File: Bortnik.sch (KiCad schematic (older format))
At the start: 1 part

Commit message: Up
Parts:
- added X?: СНП58-64-МПИ, symbol 180x:СНП58-64-МПИ
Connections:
- new net: X?.A2 (GND), X?.A3 (GND)
- new net: X?.B2 (GND), X?.B3 (GND)
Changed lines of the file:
@@
 	1    0    0    -1
 $EndComp
+$Comp
+L 180x:СНП58-64-МПИ X?
+U 1 1 61B01EB3
+P 2450 3675
+F 0 "X?" H 2450 5400 50  0000 C CNN
+F 1 "СНП58-64-МПИ" H 2450 5309 50  0000 C CNN
+F 2 "" H 2000 3675 50  0001 C CNN
+F 3 "" H 2000 3675 50  0001 C CNN
+	1    2450 3675
+	1    0    0    -1
+$EndComp
+Text GLabel 1225 4050 0    50   BiDi ~ 0
+IRQ3
+Text GLabel 1225 4175 0    50   BiDi ~ 0
+IRQ2
+Text GLabel 1225 4300 0    50   BiDi ~ 0
+IRQ1
+Text GLabel 1225 4425 0    50   BiDi ~ 0
+IRQ0
+Wire Wire Line
+	2950 2275 3100 2275
+Wire Wire Line
+	3100 2275 3100 2375
+Wire Wire Line
+	3100 2375 2950 2375
+Wire Wire Line
+	1950 2275 1825 2275
+Wire Wire Line
+	1825 2275 1825 2375
+Wire Wire Line
+	1825 2375 1950 2375
 $EndSCHEMATC

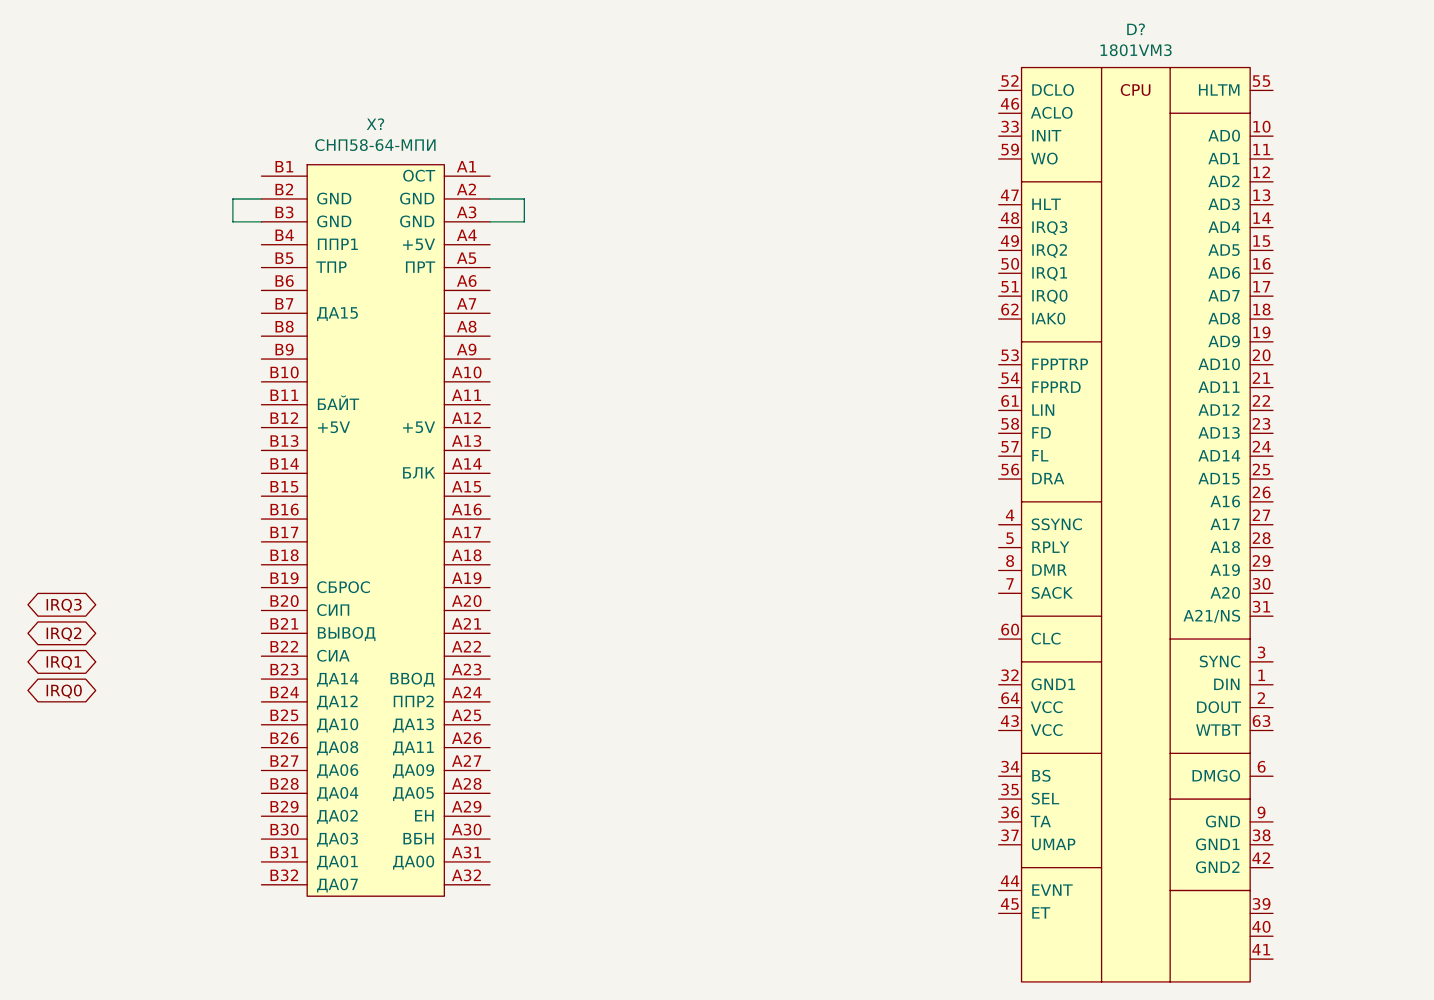
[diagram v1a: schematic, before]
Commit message: Update for Peripheral connector
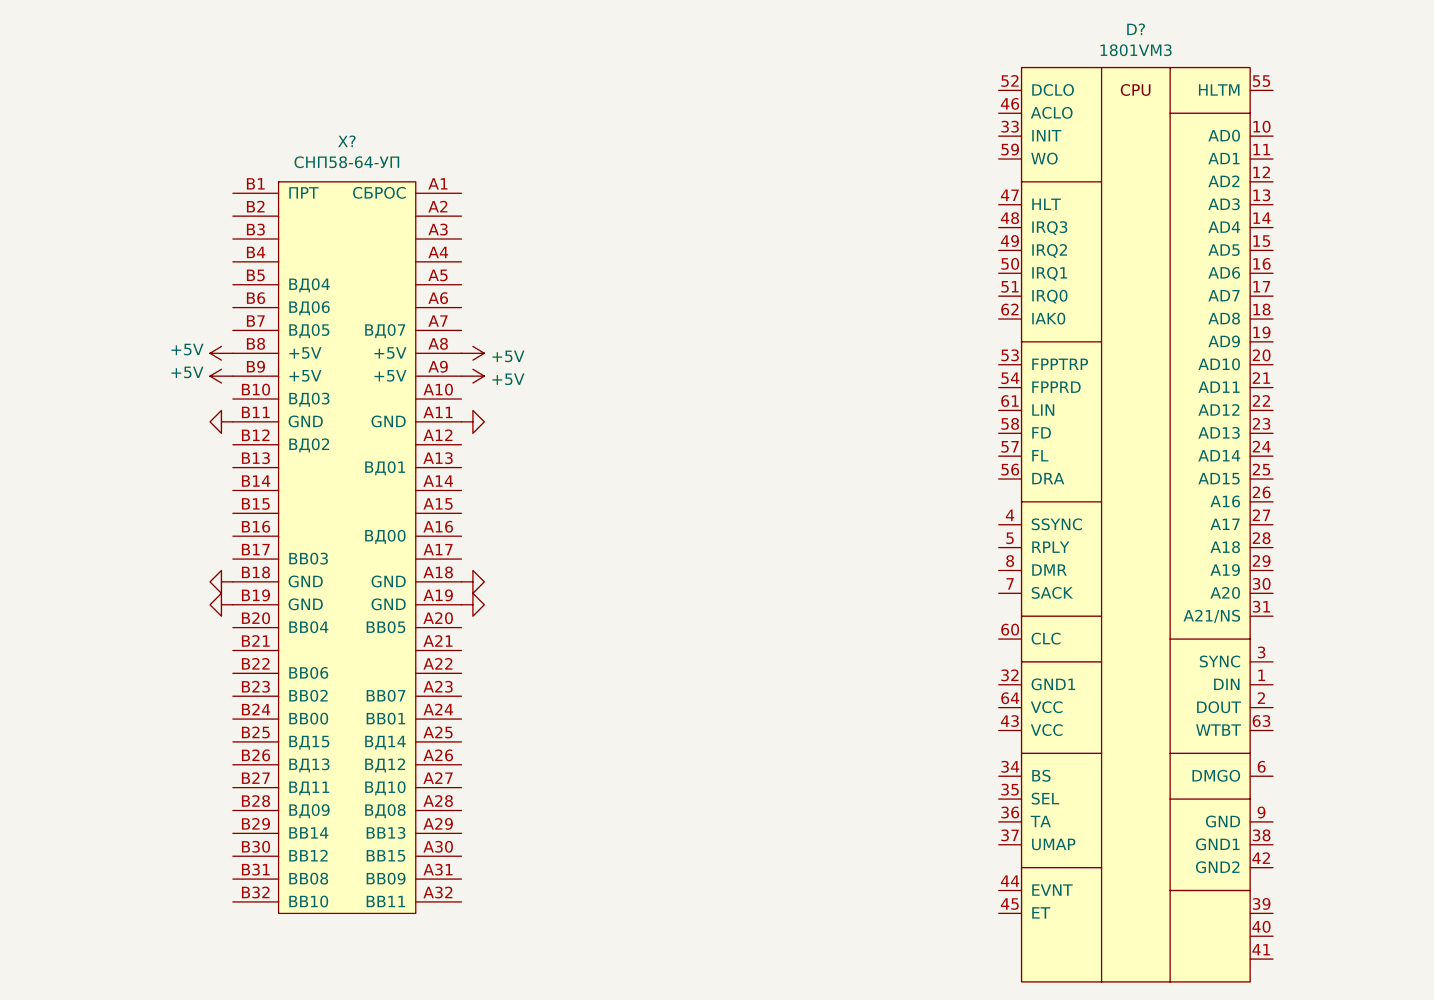
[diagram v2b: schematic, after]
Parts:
- removed X?: СНП58-64-МПИ, symbol 180x:СНП58-64-МПИ
- added X?: СНП58-64-УП, symbol 180x:СНП58-64-УП
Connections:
- new net +5V: X?.A8 (+5V), X?.A9 (+5V), X?.B8 (+5V), X?.B9 (+5V)
- new net GND: X?.A11 (GND), X?.A18 (GND), X?.A19 (GND), X?.B11 (GND), X?.B18 (GND), X?.B19 (GND)
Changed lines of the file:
@@
 $EndComp
 $Comp
-L 180x:СНП58-64-МПИ X?
-U 1 1 61B01EB3
-P 2450 3675
-F 0 "X?" H 2450 5400 50  0000 C CNN
-F 1 "СНП58-64-МПИ" H 2450 5309 50  0000 C CNN
-F 2 "" H 2000 3675 50  0001 C CNN
-F 3 "" H 2000 3675 50  0001 C CNN
-	1    2450 3675
+L power:+5V #PWR?
+U 1 1 61B662BF
+P 1825 3050
+F 0 "#PWR?" H 1825 2900 50  0001 C CNN
+F 1 "+5V" V 1840 3178 50  0000 L CNN
+F 2 "" H 1825 3050 50  0001 C CNN
+F 3 "" H 1825 3050 50  0001 C CNN
+	1    1825 3050
+	0    -1   -1   0
+$EndComp
+$Comp
+L power:+5V #PWR?
+U 1 1 61B65EB9
+P 1825 2950
+F 0 "#PWR?" H 1825 2800 50  0001 C CNN
+F 1 "+5V" V 1840 3078 50  0000 L CNN
+F 2 "" H 1825 2950 50  0001 C CNN
+F 3 "" H 1825 2950 50  0001 C CNN
+	1    1825 2950
+	0    -1   -1   0
+$EndComp
+$Comp
+L power:+5V #PWR?
+U 1 1 61B6590B
+P 2825 3050
+F 0 "#PWR?" H 2825 2900 50  0001 C CNN
+F 1 "+5V" V 2840 3178 50  0000 L CNN
+F 2 "" H 2825 3050 50  0001 C CNN
+F 3 "" H 2825 3050 50  0001 C CNN
+	1    2825 3050
+	0    1    1    0
+$EndComp
+$Comp
+L power:+5V #PWR?
+U 1 1 61B63F49
+P 2825 2950
+F 0 "#PWR?" H 2825 2800 50  0001 C CNN
+F 1 "+5V" V 2840 3078 50  0000 L CNN
+F 2 "" H 2825 2950 50  0001 C CNN
+F 3 "" H 2825 2950 50  0001 C CNN
+	1    2825 2950
+	0    1    1    0
+$EndComp
+$Comp
+L power:GND #PWR?
+U 1 1 61B636D2
+P 1825 3250
+F 0 "#PWR?" H 1825 3000 50  0001 C CNN
+F 1 "GND" H 1830 3077 50  0001 C CNN
+F 2 "" H 1825 3250 50  0001 C CNN
+F 3 "" H 1825 3250 50  0001 C CNN
+	1    1825 3250
+	0    1    1    0
+$EndComp
+$Comp
+L power:GND #PWR?
+U 1 1 61B63258
+P 1825 4050
+F 0 "#PWR?" H 1825 3800 50  0001 C CNN
+F 1 "GND" H 1830 3877 50  0001 C CNN
+F 2 "" H 1825 4050 50  0001 C CNN
+F 3 "" H 1825 4050 50  0001 C CNN
+	1    1825 4050
+	0    1    1    0
+$EndComp
+$Comp
+L power:GND #PWR?
+U 1 1 61B63006
+P 1825 3950
+F 0 "#PWR?" H 1825 3700 50  0001 C CNN
+F 1 "GND" H 1830 3777 50  0001 C CNN
+F 2 "" H 1825 3950 50  0001 C CNN
+F 3 "" H 1825 3950 50  0001 C CNN
+	1    1825 3950
+	0    1    1    0
+$EndComp
+$Comp
+L power:GND #PWR?
+U 1 1 61B62786
+P 2825 4050
+F 0 "#PWR?" H 2825 3800 50  0001 C CNN
+F 1 "GND" H 2830 3877 50  0001 C CNN
+F 2 "" H 2825 4050 50  0001 C CNN
+F 3 "" H 2825 4050 50  0001 C CNN
+	1    2825 4050
+	0    -1   -1   0
+$EndComp
+$Comp
+L power:GND #PWR?
+U 1 1 61B62052
+P 2825 3950
+F 0 "#PWR?" H 2825 3700 50  0001 C CNN
+F 1 "GND" H 2830 3777 50  0001 C CNN
+F 2 "" H 2825 3950 50  0001 C CNN
+F 3 "" H 2825 3950 50  0001 C CNN
+	1    2825 3950
+	0    -1   -1   0
+$EndComp
+$Comp
+L power:GND #PWR?
+U 1 1 61B615CA
+P 2825 3250
+F 0 "#PWR?" H 2825 3000 50  0001 C CNN
+F 1 "GND" H 2830 3077 50  0001 C CNN
+F 2 "" H 2825 3250 50  0001 C CNN
+F 3 "" H 2825 3250 50  0001 C CNN
+	1    2825 3250
+	0    -1   -1   0
+$EndComp
+$Comp
+L 180x:СНП58-64-УП X?
+U 1 1 61B5F05E
+P 2325 3750
+F 0 "X?" H 2325 5475 50  0000 C CNN
+F 1 "СНП58-64-УП" H 2325 5384 50  0000 C CNN
+F 2 "" H 1875 3750 50  0001 C CNN
+F 3 "" H 1875 3750 50  0001 C CNN
+	1    2325 3750
 	1    0    0    -1
 $EndComp
-Text GLabel 1225 4050 0    50   BiDi ~ 0
-IRQ3
-Text GLabel 1225 4175 0    50   BiDi ~ 0
-IRQ2
-Text GLabel 1225 4300 0    50   BiDi ~ 0
-IRQ1
-Text GLabel 1225 4425 0    50   BiDi ~ 0
-IRQ0
-Wire Wire Line
-	2950 2275 3100 2275
-Wire Wire Line
-	3100 2275 3100 2375
-Wire Wire Line
-	3100 2375 2950 2375
-Wire Wire Line
-	1950 2275 1825 2275
-Wire Wire Line
-	1825 2275 1825 2375
-Wire Wire Line
-	1825 2375 1950 2375
 $EndSCHEMATC

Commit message: Update Bortnik.sch
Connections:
- net GND: now also D?.59 (WO)
- net 32-DIN: now reaches D?.1 (DIN)
- net 1-AD00: now reaches D?.10 (AD0)
- net 2-AD01: now reaches D?.11 (AD1)
- net 3-AD02: now reaches D?.12 (AD2)
- net 4-AD03: now reaches D?.13 (AD3)
- net 5-AD04: now reaches D?.14 (AD4)
- net 6-AD05: now reaches D?.15 (AD5)
- net 7-AD06: now reaches D?.16 (AD6)
- net 8-AD07: now reaches D?.17 (AD7)
- net 9-AD08: now reaches D?.18 (AD8)
- net 10-AD09: now reaches D?.19 (AD9)
- net 33-DOUT: now reaches D?.2 (DOUT)
- net 11-AD10: now reaches D?.20 (AD10)
- net 12-AD11: now reaches D?.21 (AD11)
- net 13-AD12: now reaches D?.22 (AD12)
- net 14-AD13: now reaches D?.23 (AD13)
- net 15-AD14: now reaches D?.24 (AD14)
- net 16-AD15: now reaches D?.25 (AD15)
- net 17-AD16: now reaches D?.26 (A16)
- net 18-AD17: now reaches D?.27 (A17)
- net 19-AD18: now reaches D?.28 (A18)
- net 20-AD19: now reaches D?.29 (A19)
- net 31-SYNC: now reaches D?.3 (SYNC)
- net 21-AD20: now reaches D?.30 (A20)
- net 22-AD21: now reaches D?.31 (A21/NS)
- net 24-BS: now reaches D?.34 (BS)
- net EVNT: now reaches D?.44 (EVNT)
- net 31: now reaches D?.46 (ACLO)
- net 31: now also X?.A25 (ВД14)
- net 26: now reaches D?.48 (IRQ3)
- net 26: now also X?.B28 (ВД09)
- net 27: now reaches D?.49 (IRQ2)
- net 27: now also X?.A27 (ВД10)
- net 36-RPLY: now reaches D?.5 (RPLY)
- net 28: now reaches D?.50 (IRQ1)
- net 28: now also X?.B27 (ВД11)
- net 25: now reaches D?.51 (IRQ0)
- net 25: now also X?.A28 (ВД08)
- net 30: now reaches D?.52 (DCLO)
- net 30: now also X?.B26 (ВД13)
- net 35-6MHZ: now reaches D?.60 (CLC)
- net 35-IAK: now reaches D?.62 (IAK0)
- net 34-WTBT: now reaches D?.63 (WTBT)
- net 18: now reaches X?.A13 (ВД01)
- net 17: now reaches X?.A16 (ВД00)
- net 6: now reaches X?.A20 (ВВ05)
- net 8: now reaches X?.A23 (ВВ07)
- net 2: now reaches X?.A24 (ВВ01)
- net 29: now reaches X?.A26 (ВД12)
- net 14: now reaches X?.A29 (ВВ13)
- net 16: now reaches X?.A30 (ВВ15)
- net 10: now reaches X?.A31 (ВВ09)
- net 12: now reaches X?.A32 (ВВ11)
- net 24: now reaches X?.A7 (ВД07)
- net 20: now reaches X?.B10 (ВД03)
- net 19: now reaches X?.B12 (ВД02)
- net 4: now reaches X?.B17 (ВВ03)
- net 5: now reaches X?.B20 (ВВ04)
- net 7: now reaches X?.B22 (ВВ06)
- net 3: now reaches X?.B23 (ВВ02)
- net 1: now reaches X?.B24 (ВВ00)
- net 32: now reaches X?.B25 (ВД15)
- net 15: now reaches X?.B29 (ВВ14)
- net 13: now reaches X?.B30 (ВВ12)
- net 9: now reaches X?.B31 (ВВ08)
- net 11: now reaches X?.B32 (ВВ10)
- net 21: now reaches X?.B5 (ВД04)
- net 23: now reaches X?.B6 (ВД06)
- net 22: now reaches X?.B7 (ВД05)
